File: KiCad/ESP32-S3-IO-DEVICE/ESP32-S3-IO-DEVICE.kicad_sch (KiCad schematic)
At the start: 62 parts, among them J1 Terminal_04, J2 Terminal_04, J3 Terminal_06, J4 Terminal_02, J5 Terminal_04, J6 Terminal_06, Q1 2SC1815, Q10 2SC1815, Q11 2SC1815, Q12 2SC1815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

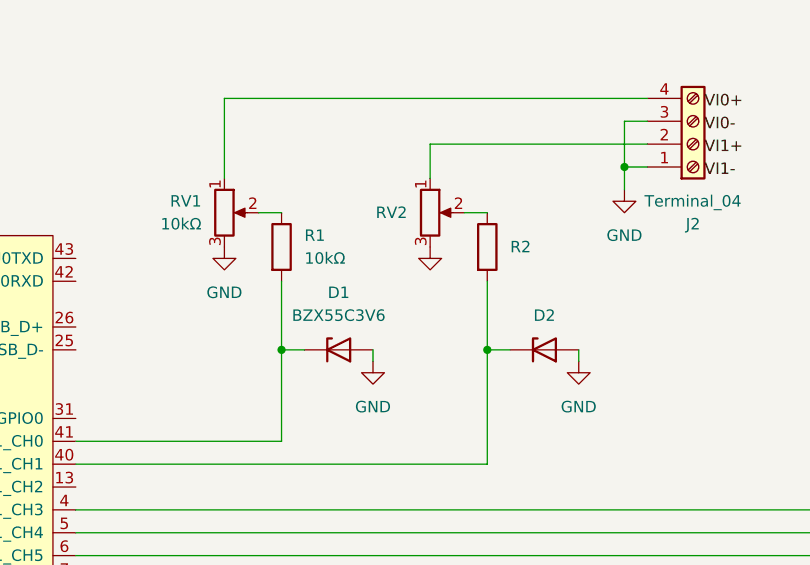
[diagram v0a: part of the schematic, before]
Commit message: Update schematic: fix wiring errors and improve component labeling
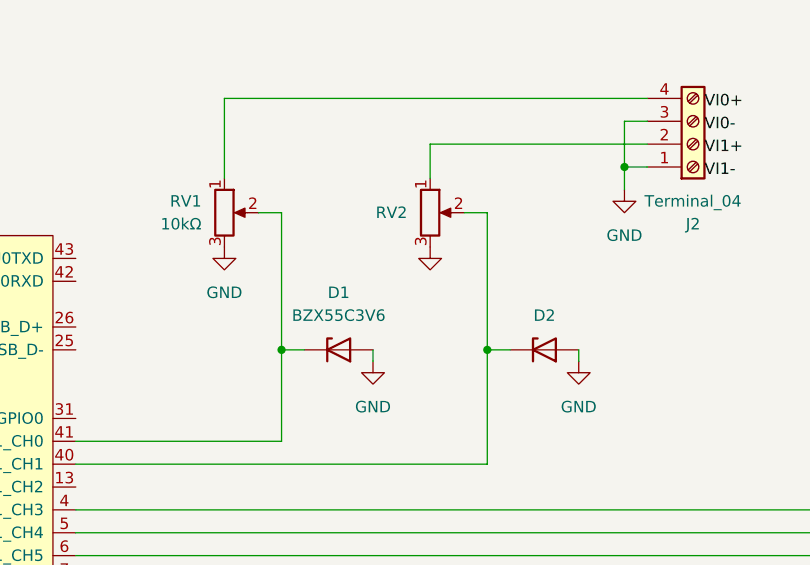
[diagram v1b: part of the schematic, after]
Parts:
- removed R1, R2: 10kΩ, Resistor_THT:R_Axial_DIN0207_L6.3mm_D2.5mm_P7.62mm_Horizontal, symbol Device:R
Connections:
- net at RV1.2: now also D1.1 (K), U1.41 (GPIO1/ADC1_CH0)
- net at RV2.2: now also D2.1 (K), U1.40 (GPIO2/ADC1_CH1)
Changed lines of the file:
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@@
 	(wire
 		(pts
-			(xy 97.79 43.18) (xy 97.79 50.8)
-		)
-		(stroke
-			(width 0)
-			(type default)
-		)
-	)
-	(wire
-		(pts
 			(xy 95.25 35.56) (xy 97.79 35.56)
 		)
@@
 	(wire
 		(pts
+			(xy 97.79 35.56) (xy 97.79 50.8)
+		)
+		(stroke
+			(width 0)
+			(type default)
+		)
+	)
+	(wire
+		(pts
 			(xy 195.58 83.82) (xy 195.58 86.36)
 		)
@@
 	(wire
 		(pts
-			(xy 120.65 43.18) (xy 120.65 50.8)
+			(xy 120.65 35.56) (xy 120.65 50.8)
 		)
 		(stroke
@@
 	)
 	(symbol
-		(lib_id "Device:R")
-		(at 120.65 39.37 0)
-		(unit 1)
-		(exclude_from_sim no)
-		(in_bom yes)
-		(on_board yes)
-		(dnp no)
-		(fields_autoplaced yes)
-		(property "Reference" "R2"
-			(at 123.19 39.3699 0)
-			(effects
-				(font
-					(size 1.27 1.27)
-				)
-				(justify left)
-			)
-		)
-		(property "Value" "10kΩ"
-			(at 123.19 40.6399 0)
-			(effects
-				(font
-					(size 1.27 1.27)
-				)
-				(justify left)
-				(hide yes)
-			)
-		)
-		(property "Footprint" "Resistor_THT:R_Axial_DIN0207_L6.3mm_D2.5mm_P7.62mm_Horizontal"
-			(at 118.872 39.37 90)
-			(effects
-				(font
-					(size 1.27 1.27)
-				)
-				(hide yes)
-			)
-		)
-		(property "Datasheet" "~"
-			(at 120.65 39.37 0)
-			(effects
-				(font
-					(size 1.27 1.27)
-				)
-				(hide yes)
-			)
-		)
-		(property "Description" "Resistor"
-			(at 120.65 39.37 0)
-			(effects
-				(font
-					(size 1.27 1.27)
-				)
-				(hide yes)
-			)
-		)
-		(pin "2"
-		)
-		(pin "1"
-		)
-		(instances
-			(project "ESP32-S3-IO-DEVICE"
-				(path "/14e24596-d690-4281-a3cc-ee23062842b6"
-					(reference "R2")
-					(unit 1)
-				)
-			)
-		)
-	)
-	(symbol
 		(lib_id "power:GND")
 		(at 91.44 39.37 0)
@@
 					(unit 1)
 				)
-			)
-		)
-	)
-	(symbol
-		(lib_id "Device:R")
-		(at 97.79 39.37 0)
-		(unit 1)
-		(exclude_from_sim no)
-		(in_bom yes)
-		(on_board yes)
-		(dnp no)
-		(fields_autoplaced yes)
-		(property "Reference" "R1"
-			(at 100.33 38.0999 0)
-			(effects
-				(font
-					(size 1.27 1.27)
-				)
-				(justify left)
-			)
-		)
-		(property "Value" "10kΩ"
-			(at 100.33 40.6399 0)
-			(effects
-				(font
-					(size 1.27 1.27)
-				)
-				(justify left)
-			)
-		)
-		(property "Footprint" "Resistor_THT:R_Axial_DIN0207_L6.3mm_D2.5mm_P7.62mm_Horizontal"
-			(at 96.012 39.37 90)
-			(effects
-				(font
-					(size 1.27 1.27)
-				)
-				(hide yes)
-			)
-		)
-		(property "Datasheet" "~"
-			(at 97.79 39.37 0)
-			(effects
-				(font
-					(size 1.27 1.27)
-				)
-				(hide yes)
-			)
-		)
-		(property "Description" "Resistor"
-			(at 97.79 39.37 0)
-			(effects
-				(font
-					(size 1.27 1.27)
-				)
-				(hide yes)
-			)
-		)
-		(pin "2"
-		)
-		(pin "1"
-		)
-		(instances
-			(project "ESP32-S3-IO-DEVICE"
-				(path "/14e24596-d690-4281-a3cc-ee23062842b6"
-					(reference "R1")
-					(unit 1)
-				)
